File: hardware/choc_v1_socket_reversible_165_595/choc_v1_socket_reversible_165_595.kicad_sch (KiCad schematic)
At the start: 70 parts, among them SW00 SW_Push, SW01 SW_Push, SW02 SW_Push, SW03 SW_Push, SW04 SW_Push, SW05 SW_Push, SW10 SW_Push, SW11 SW_Push, SW12 SW_Push, SW13 SW_Push, SW14 SW_Push, SW15 SW_Push, SW20 SW_Push, SW21 SW_Push, SW22 SW_Push, SW23 SW_Push, SW24 SW_Push, SW25 SW_Push, SW26 SW_Push, SW30 SW_Push, SW31 SW_Push, SW32 SW_Push, SW33 SW_Push, SW34 SW_Push, SW35 SW_Push, SW36 SW_Push, U1 CH582

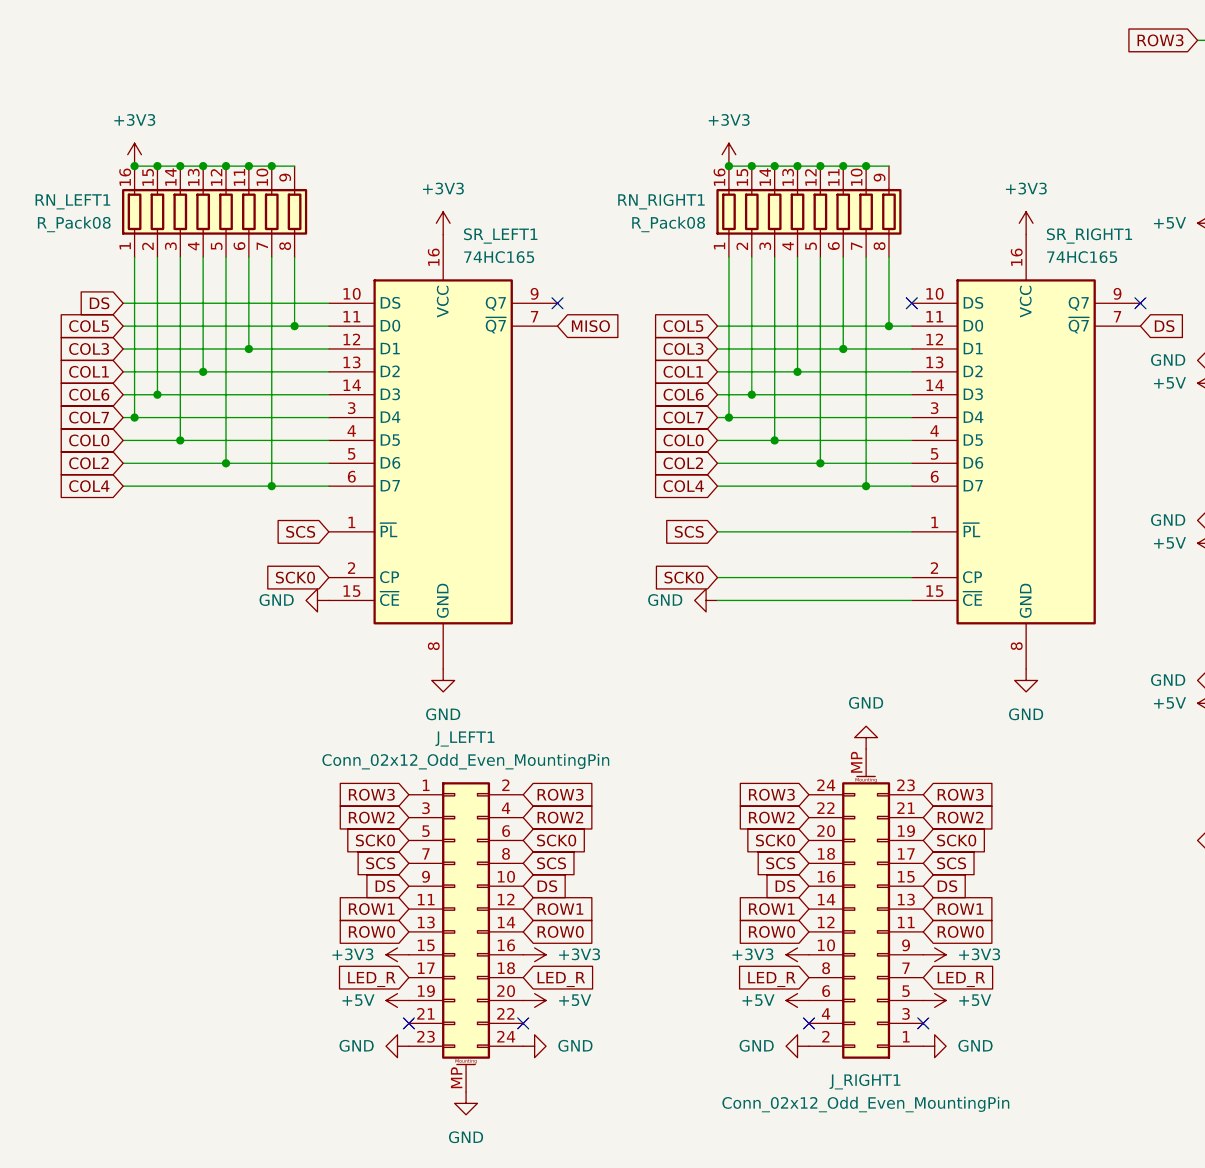
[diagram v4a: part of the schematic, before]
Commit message: Updated schematic to use 0805 ressitor and 1x12 FFC socket
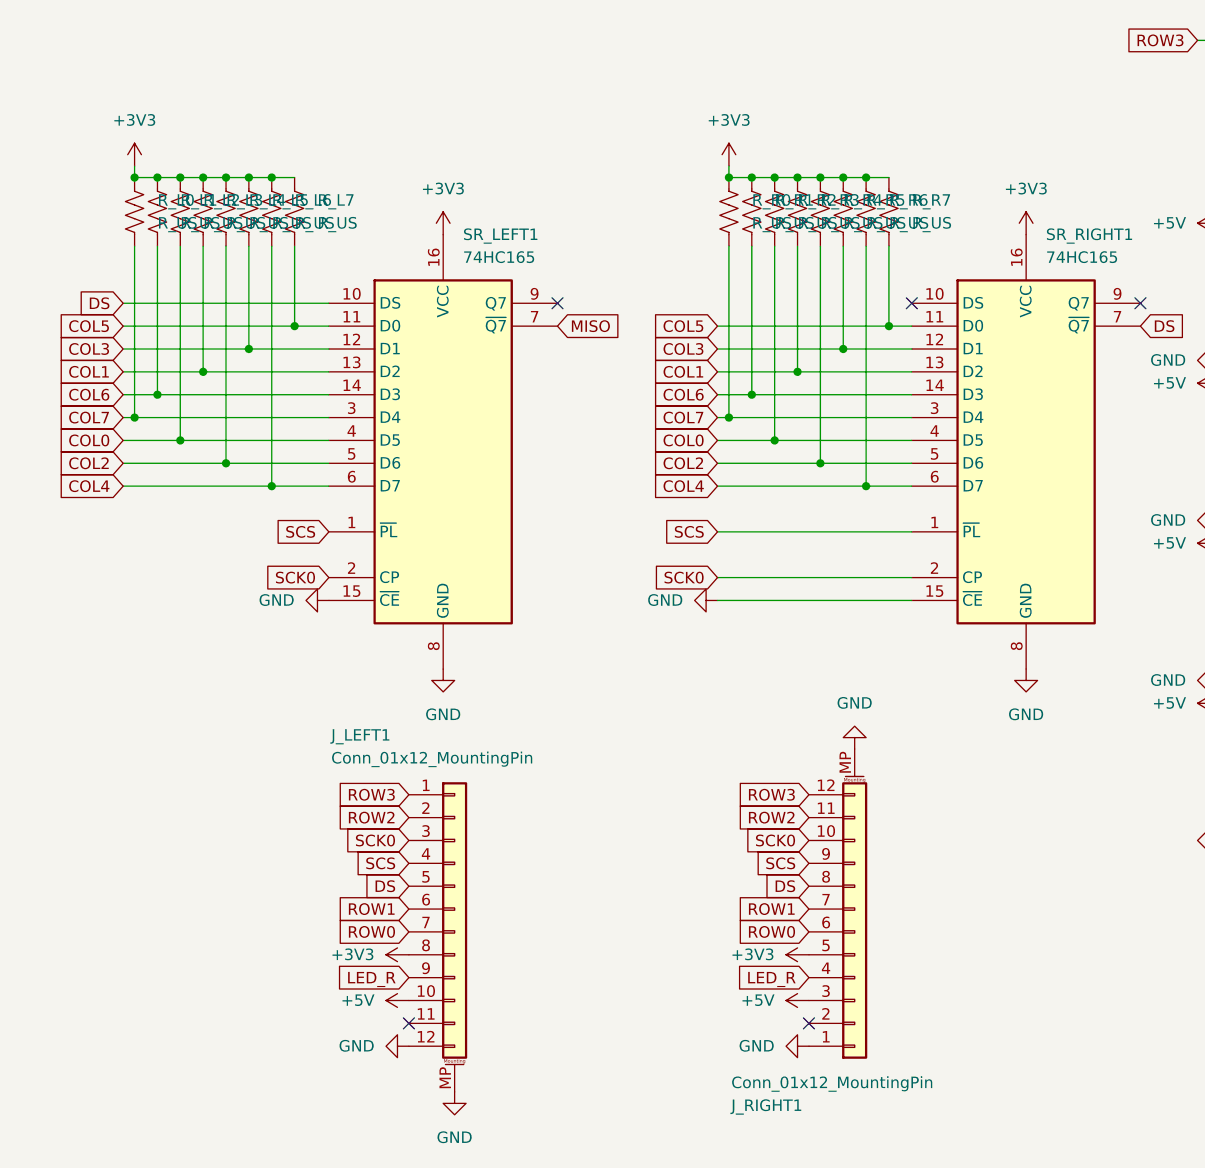
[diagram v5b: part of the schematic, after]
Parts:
- removed J_LEFT1, J_RIGHT1: Conn_02x12_Odd_Even_MountingPin, Connector_FFC-FPC:Jushuo_AFC07-S24FCA-00_1x24-1MP_P0.50_Horizontal, symbol Connector_Generic_MountingPin:Conn_02x12_Odd_Even_MountingPin
- removed RN_LEFT1, RN_RIGHT1: R_Pack08, Resistor_SMD:R_Array_Convex_8x0602, symbol Device:R_Pack08
- added J_LEFT1, J_RIGHT1: Conn_01x12_MountingPin, symbol Connector_Generic_MountingPin:Conn_01x12_MountingPin
- added R_L0, R_L1, R_L2, R_L3, R_L4, R_L5, R_L6, R_L7, R_R0, R_R1, R_R2, R_R3, R_R4, R_R5, R_R6, R_R7: R_US, Resistor_SMD:R_0805_2012Metric_Pad1.20x1.40mm_HandSolder, symbol Device:R_US
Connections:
- net +3V3: now also J_LEFT1.8 (Pin_8), J_RIGHT1.5 (Pin_5), R_L0.1, R_L1.1, R_L2.1, R_L3.1, R_L4.1, R_L5.1, R_L6.1, R_L7.1, R_R0.1, R_R1.1, R_R2.1, R_R3.1, R_R4.1, R_R5.1, R_R6.1, R_R7.1
- net +5V: now also J_LEFT1.10 (Pin_10), J_RIGHT1.3 (Pin_3)
- net COL0: now also R_L2.2, R_R2.2
- net COL1: now also R_L3.2, R_R3.2
- net COL2: now also R_L4.2, R_R4.2
- net COL3: now also R_L5.2, R_R5.2
- net COL4: now also R_L6.2, R_R6.2
- net COL5: now also R_L7.2, R_R7.2
- net COL6: now also R_L1.2, R_R1.2
- net COL7: now also R_L0.2, R_R0.2
- net DS: now also J_LEFT1.5 (Pin_5), J_RIGHT1.8 (Pin_8)
- net GND: now also J_LEFT1.12 (Pin_12), J_LEFT1.MP (MountPin), J_RIGHT1.1 (Pin_1), J_RIGHT1.MP (MountPin)
- net LED_R: now also J_LEFT1.9 (Pin_9), J_RIGHT1.4 (Pin_4)
- net ROW0: now also J_LEFT1.7 (Pin_7), J_RIGHT1.6 (Pin_6)
- net ROW1: now also J_LEFT1.6 (Pin_6), J_RIGHT1.7 (Pin_7)
- net ROW2: now also J_LEFT1.2 (Pin_2), J_RIGHT1.11 (Pin_11)
- net ROW3: now also J_LEFT1.1 (Pin_1), J_RIGHT1.12 (Pin_12)
- net SCK0: now also J_LEFT1.3 (Pin_3), J_RIGHT1.10 (Pin_10)
- net SCS: now also J_LEFT1.4 (Pin_4), J_RIGHT1.9 (Pin_9)
- no-connect marks 19 -> 17

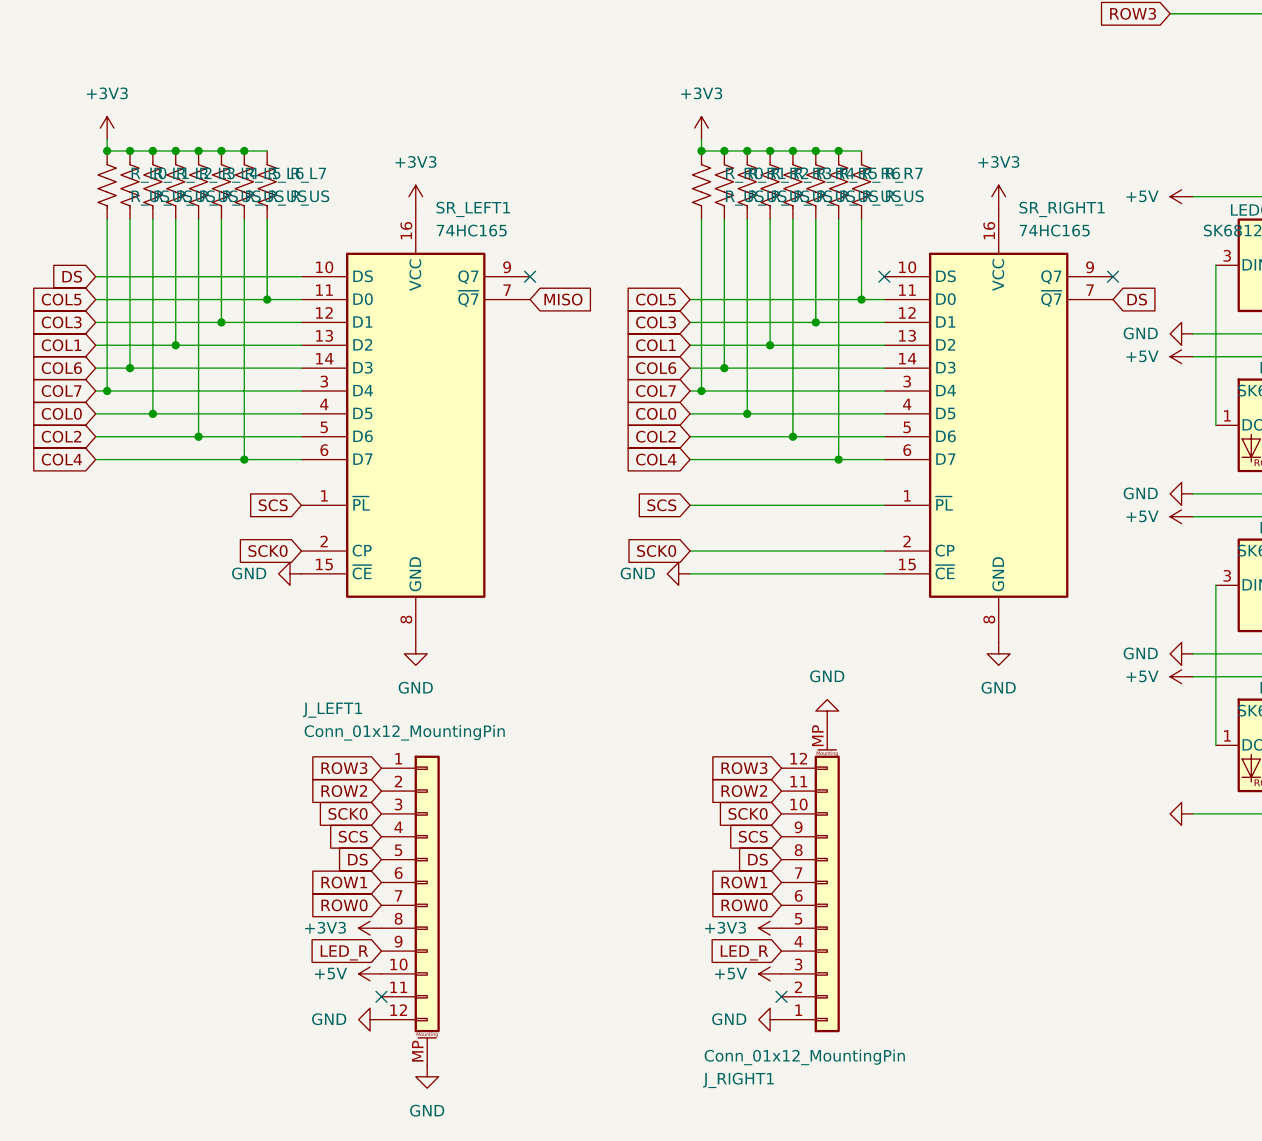
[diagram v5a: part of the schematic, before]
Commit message: Updated connector and resistor for easier SMD soldering
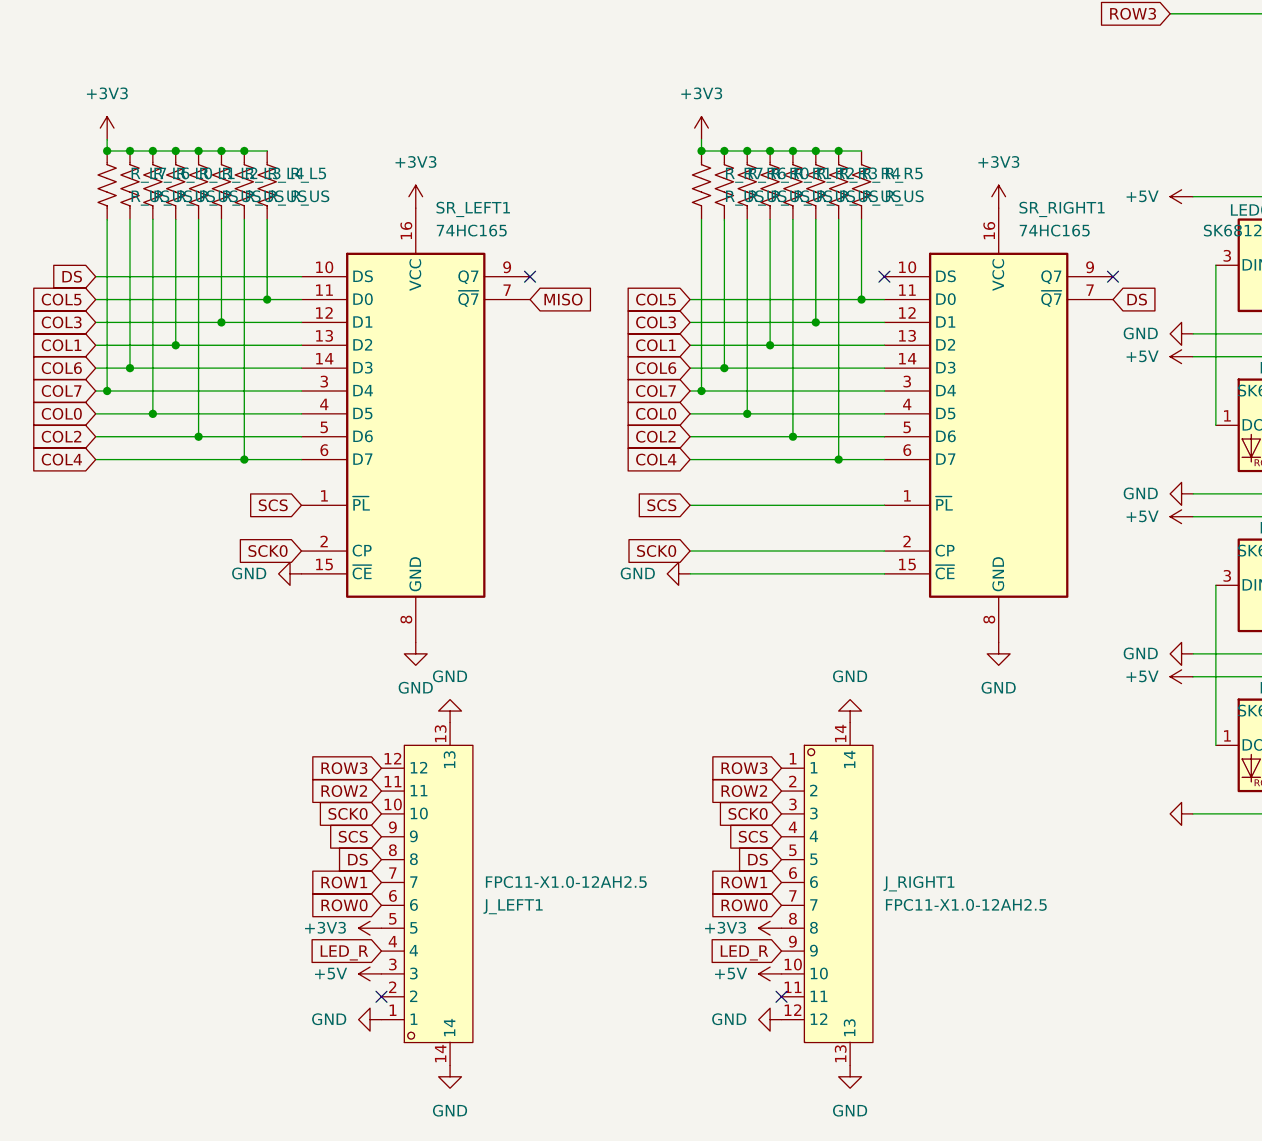
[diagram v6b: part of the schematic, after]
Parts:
- removed J_LEFT1, J_RIGHT1: Conn_01x12_MountingPin, symbol Connector_Generic_MountingPin:Conn_01x12_MountingPin
- added J_LEFT1, J_RIGHT1: FPC11-X1.0-12AH2.5, easyeda2kicad:FPC-SMD_12P-P1.00_XYECONN_FPC10-S1.0-12AH2.5, symbol easyeda2kicad:FPC11-X1.0-12AH2.5
- renumbered R_L2 to R_L0, R_L3 to R_L1, R_L4 to R_L2, R_L5 to R_L3, R_L6 to R_L4, R_L7 to R_L5, R_L1 to R_L6, R_L0 to R_L7, R_R2 to R_R0, R_R3 to R_R1, R_R4 to R_R2, R_R5 to R_R3, R_R6 to R_R4, R_R7 to R_R5, R_R1 to R_R6, R_R0 to R_R7
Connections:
- net +3V3: now also J_LEFT1.5, J_RIGHT1.8
- net +5V: now also J_LEFT1.3, J_RIGHT1.10
- net DS: now also J_LEFT1.8, J_RIGHT1.5
- net GND: now also J_LEFT1.1, J_LEFT1.13, J_LEFT1.14, J_RIGHT1.12, J_RIGHT1.13, J_RIGHT1.14
- net LED_R: now also J_LEFT1.4, J_RIGHT1.9
- net ROW0: now also J_LEFT1.6, J_RIGHT1.7
- net ROW1: now also J_LEFT1.7, J_RIGHT1.6
- net ROW2: now also J_LEFT1.11, J_RIGHT1.2
- net ROW3: now also J_LEFT1.12, J_RIGHT1.1
- net SCK0: now also J_LEFT1.10, J_RIGHT1.3
- net SCS: now also J_LEFT1.9, J_RIGHT1.4

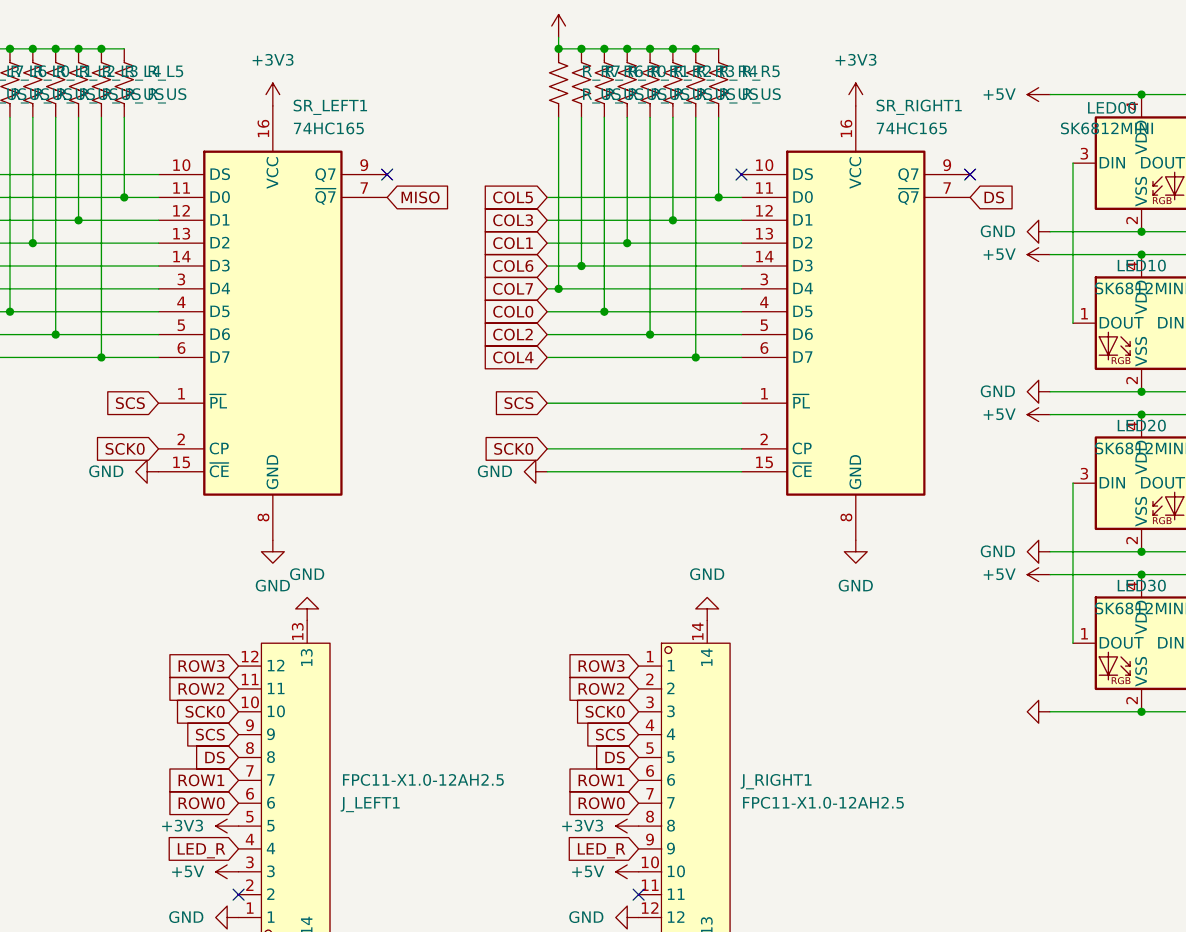
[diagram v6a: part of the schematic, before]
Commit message: Fixed SER-QH connection
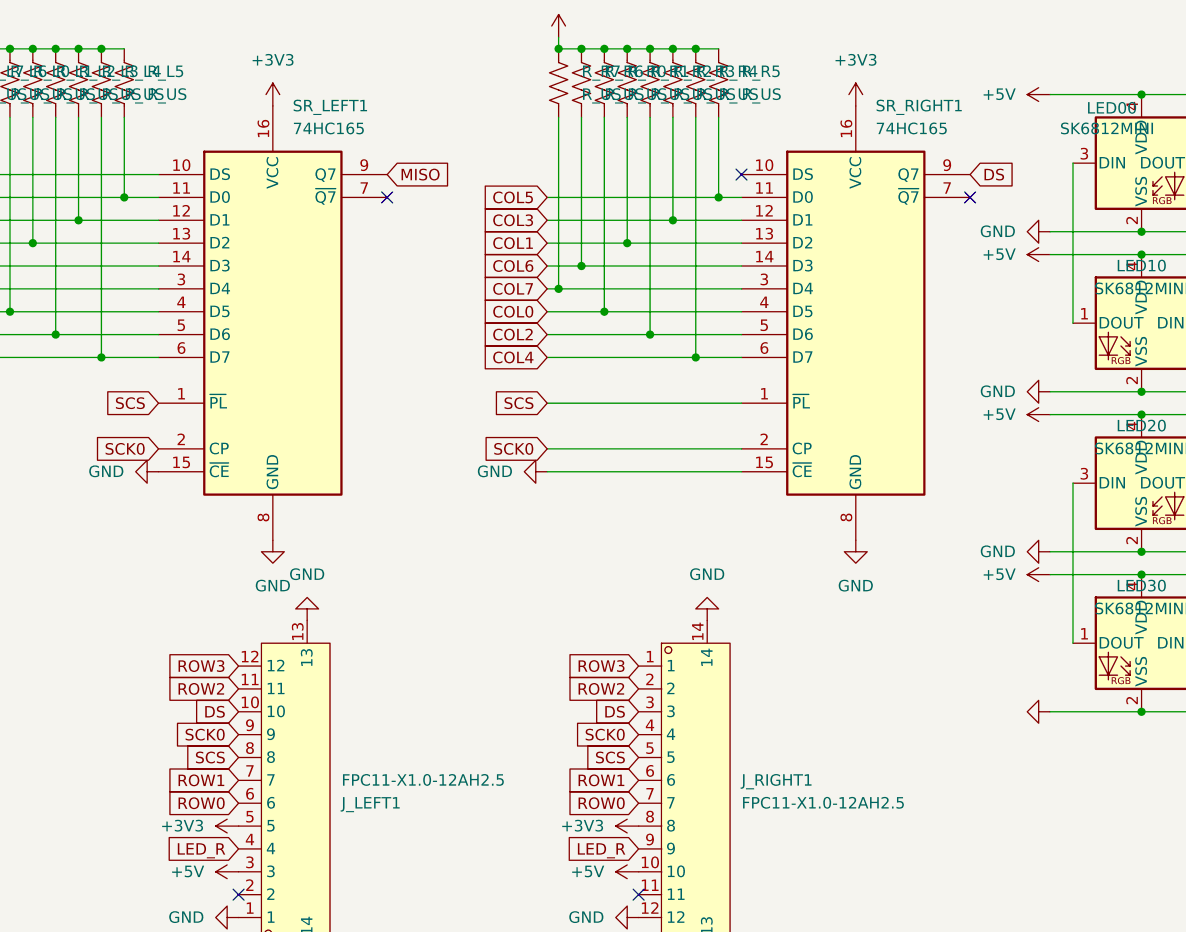
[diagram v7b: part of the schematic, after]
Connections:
- net DS: now also J_LEFT1.10, J_RIGHT1.3, SR_RIGHT1.9 (Q7); no longer J_LEFT1.8, J_RIGHT1.5, SR_RIGHT1.7 (~{Q7})
- net MISO: now also SR_LEFT1.9 (Q7); no longer SR_LEFT1.7 (~{Q7})
- net SCK0: now also J_LEFT1.9, J_RIGHT1.4; no longer J_LEFT1.10, J_RIGHT1.3
- net SCS: now also J_LEFT1.8, J_RIGHT1.5; no longer J_LEFT1.9, J_RIGHT1.4
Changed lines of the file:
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@@
 	)
 	(no_connect
-		(at 68.58 102.87)
-	)
-	(no_connect
 		(at 107.95 102.87)
 	)
@@
 	)
 	(no_connect
-		(at 133.35 102.87)
+		(at 133.35 105.41)
+	)
+	(no_connect
+		(at 68.58 105.41)
 	)
 	(no_connect
@@
 	(global_label "SCK0"
 		(shape input)
-		(at 96.52 162.56 180)
+		(at 96.52 165.1 180)
 		(fields_autoplaced yes)
 		(effects
@@
 		)
 		(property "Intersheetrefs" "${INTERSHEET_REFS}"
-			(at 88.5758 162.56 0)
+			(at 88.5758 165.1 0)
 			(effects
 				(font
@@
 	(global_label "SCK0"
 		(shape input)
-		(at 52.07 162.56 180)
+		(at 52.07 165.1 180)
 		(fields_autoplaced yes)
 		(effects
@@
 		)
 		(property "Intersheetrefs" "${INTERSHEET_REFS}"
-			(at 44.1258 162.56 0)
+			(at 44.1258 165.1 0)
 			(effects
 				(font
@@
 		)
 	)
+	(global_label "DS"
+		(shape input)
+		(at 133.35 102.87 0)
+		(fields_autoplaced yes)
+		(effects
+			(font
+				(size 1.27 1.27)
+			)
+			(justify left)
+		)
+		(property "Intersheetrefs" "${INTERSHEET_REFS}"
+			(at 138.8147 102.87 0)
+			(effects
+				(font
+					(size 1.27 1.27)
+				)
+				(justify left)
+				(hide yes)
+			)
+		)
+	)
 	(global_label "COL4"
 		(shape input)
@@
 	(global_label "DS"
 		(shape input)
-		(at 52.07 167.64 180)
+		(at 52.07 162.56 180)
 		(fields_autoplaced yes)
 		(effects
@@
 		)
 		(property "Intersheetrefs" "${INTERSHEET_REFS}"
-			(at 46.6053 167.64 0)
+			(at 46.6053 162.56 0)
 			(effects
 				(font
@@
 	(global_label "SCS"
 		(shape input)
-		(at 96.52 165.1 180)
+		(at 96.52 167.64 180)
 		(fields_autoplaced yes)
 		(effects
@@
 		)
 		(property "Intersheetrefs" "${INTERSHEET_REFS}"
-			(at 89.8458 165.1 0)
+			(at 89.8458 167.64 0)
 			(effects
 				(font
@@
 		)
 	)
-	(global_label "DS"
-		(shape input)
-		(at 133.35 105.41 0)
-		(fields_autoplaced yes)
-		(effects
-			(font
-				(size 1.27 1.27)
-			)
-			(justify left)
-		)
-		(property "Intersheetrefs" "${INTERSHEET_REFS}"
-			(at 138.8147 105.41 0)
-			(effects
-				(font
-					(size 1.27 1.27)
-				)
-				(justify left)
-				(hide yes)
-			)
-		)
-	)
 	(global_label "ROW2"
 		(shape input)
@@
 	(global_label "DS"
 		(shape input)
-		(at 96.52 167.64 180)
+		(at 96.52 162.56 180)
 		(fields_autoplaced yes)
 		(effects
@@
 		)
 		(property "Intersheetrefs" "${INTERSHEET_REFS}"
-			(at 91.0553 167.64 0)
+			(at 91.0553 162.56 0)
 			(effects
 				(font
@@
 	(global_label "SCS"
 		(shape input)
-		(at 52.07 165.1 180)
+		(at 52.07 167.64 180)
 		(fields_autoplaced yes)
 		(effects
@@
 		)
 		(property "Intersheetrefs" "${INTERSHEET_REFS}"
-			(at 45.3958 165.1 0)
+			(at 45.3958 167.64 0)
 			(effects
 				(font
@@
 	(global_label "MISO"
 		(shape input)
-		(at 68.58 105.41 0)
+		(at 68.58 102.87 0)
 		(fields_autoplaced yes)
 		(effects
@@
 		)
 		(property "Intersheetrefs" "${INTERSHEET_REFS}"
-			(at 76.1614 105.41 0)
+			(at 76.1614 102.87 0)
 			(effects
 				(font
